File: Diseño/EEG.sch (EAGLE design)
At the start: 19 parts, among them IC1 REF2033AIDDCT

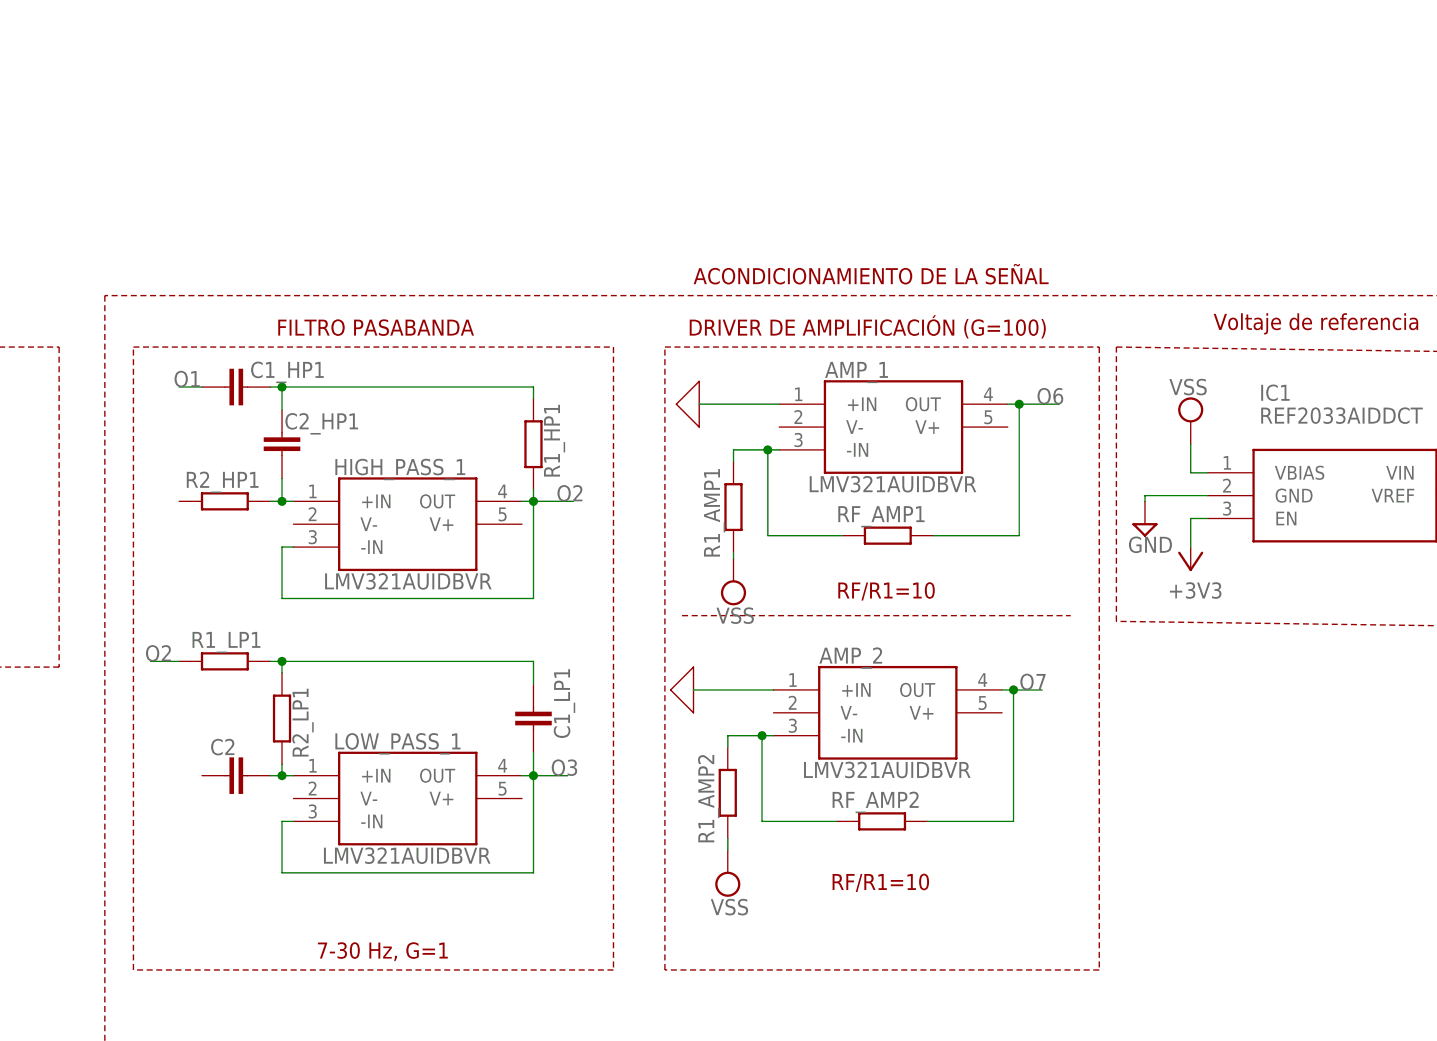
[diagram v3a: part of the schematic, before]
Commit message: correccion de tierras y entradas 3v3 añadidas (cositas varias)    v2
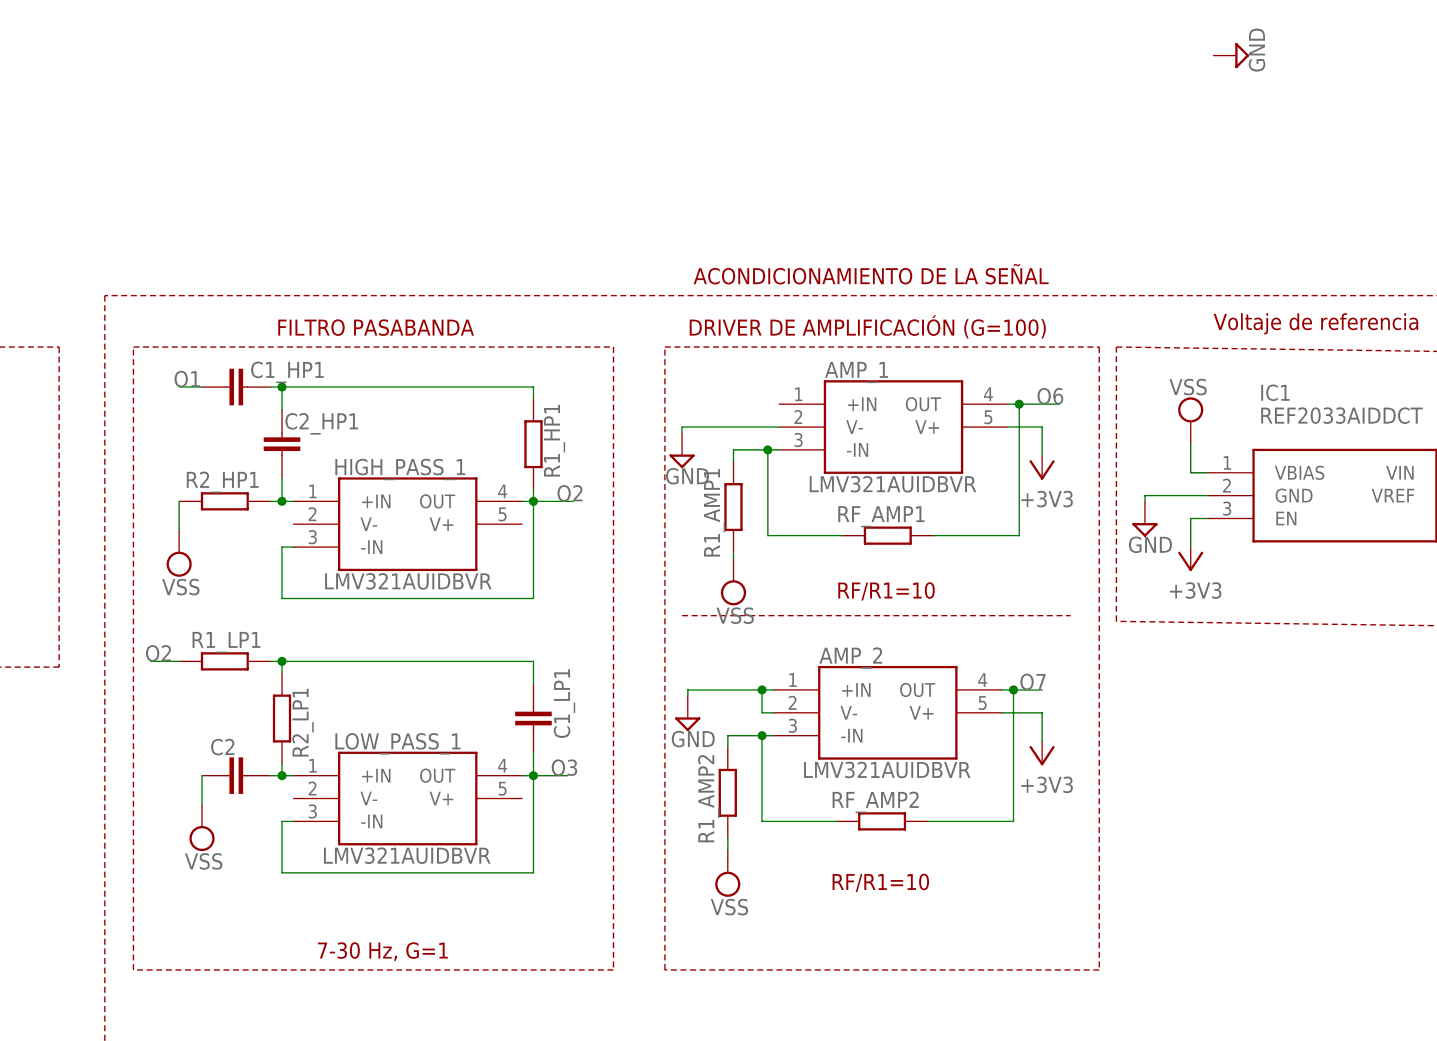
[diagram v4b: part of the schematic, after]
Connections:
- removed net 0: AMP_1.+IN, AMP_2.+IN
- net +3V3: now also AMP_1.V+, AMP_2.V+
- net GND: now also AMP_1.V-, AMP_2.+IN, AMP_2.V-
- net VSS: now also C2.2, R2_HP1.1
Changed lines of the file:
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@@
 <part name="C2" library="rcl" library_urn="urn:adsk.eagle:library:334" deviceset="C-EU" device="C0805" package3d_urn="urn:adsk.eagle:package:23617/2"/>
 <part name="AMP_1" library="LMV321AUIDBVR" deviceset="LMV321AUIDBVR" device=""/>
-<part name="X_1" library="ngspice-simulation" library_urn="urn:adsk.eagle:library:527439" deviceset="GND" device=""/>
 <part name="RF_AMP1" library="rcl" library_urn="urn:adsk.eagle:library:334" deviceset="R-EU_" device="R0805" package3d_urn="urn:adsk.eagle:package:23553/2"/>
 <part name="R1_AMP1" library="rcl" library_urn="urn:adsk.eagle:library:334" deviceset="R-EU_" device="R0805" package3d_urn="urn:adsk.eagle:package:23553/2"/>
 <part name="AMP_2" library="LMV321AUIDBVR" deviceset="LMV321AUIDBVR" device=""/>
-<part name="X_2" library="ngspice-simulation" library_urn="urn:adsk.eagle:library:527439" deviceset="GND" device=""/>
 <part name="RF_AMP2" library="rcl" library_urn="urn:adsk.eagle:library:334" deviceset="R-EU_" device="R0805" package3d_urn="urn:adsk.eagle:package:23553/2"/>
 <part name="R1_AMP2" library="rcl" library_urn="urn:adsk.eagle:library:334" deviceset="R-EU_" device="R0805" package3d_urn="urn:adsk.eagle:package:23553/2"/>
@@
 <part name="SUPPLY3" library="supply2" library_urn="urn:adsk.eagle:library:372" deviceset="VSS" device=""/>
 <part name="SUPPLY4" library="supply2" library_urn="urn:adsk.eagle:library:372" deviceset="VSS" device=""/>
+<part name="SUPPLY5" library="supply2" library_urn="urn:adsk.eagle:library:372" deviceset="GND" device=""/>
+<part name="SUPPLY6" library="supply2" library_urn="urn:adsk.eagle:library:372" deviceset="GND" device=""/>
+<part name="SUPPLY7" library="supply2" library_urn="urn:adsk.eagle:library:372" deviceset="GND" device=""/>
+<part name="+3V3" library="supply1" library_urn="urn:adsk.eagle:library:371" deviceset="+3V3" device=""/>
+<part name="+3V4" library="supply1" library_urn="urn:adsk.eagle:library:371" deviceset="+3V3" device=""/>
+<part name="SUPPLY8" library="supply2" library_urn="urn:adsk.eagle:library:372" deviceset="VSS" device=""/>
+<part name="SUPPLY9" library="supply2" library_urn="urn:adsk.eagle:library:372" deviceset="VSS" device=""/>
 </parts>
 <sheets>
@@
 <attribute name="VALUE" x="151.13" y="153.67" size="1.778" layer="96" align="center-left"/>
 </instance>
-<instance part="X_1" gate="G$1" x="139.065" y="162.56" smashed="yes" rot="R270"/>
 <instance part="RF_AMP1" gate="G$1" x="160.02" y="147.955" smashed="yes">
 <attribute name="NAME" x="154.305" y="149.4536" size="1.778" layer="95"/>
@@
 <attribute name="VALUE" x="150.495" y="121.92" size="1.778" layer="96" align="center-left"/>
 </instance>
-<instance part="X_2" gate="G$1" x="138.43" y="130.81" smashed="yes" rot="R270"/>
 <instance part="RF_AMP2" gate="G$1" x="159.385" y="116.205" smashed="yes">
 <attribute name="NAME" x="153.67" y="117.7036" size="1.778" layer="95"/>
@@
 <instance part="SUPPLY4" gate="G$1" x="142.24" y="110.49" smashed="yes">
 <attribute name="VALUE" x="140.335" y="105.791" size="1.778" layer="96"/>
+</instance>
+<instance part="SUPPLY5" gate="GND" x="198.755" y="201.295" smashed="yes" rot="R90">
+<attribute name="VALUE" x="201.93" y="199.39" size="1.778" layer="96" rot="R90"/>
+</instance>
+<instance part="SUPPLY6" gate="GND" x="137.795" y="127.635" smashed="yes">
+<attribute name="VALUE" x="135.89" y="124.46" size="1.778" layer="96"/>
+</instance>
+<instance part="SUPPLY7" gate="GND" x="137.16" y="156.845" smashed="yes">
+<attribute name="VALUE" x="135.255" y="153.67" size="1.778" layer="96"/>
+</instance>
+<instance part="+3V3" gate="G$1" x="177.165" y="154.305" smashed="yes" rot="R180">
+<attribute name="VALUE" x="174.625" y="151.13" size="1.778" layer="96"/>
+</instance>
+<instance part="+3V4" gate="G$1" x="177.165" y="122.555" smashed="yes" rot="R180">
+<attribute name="VALUE" x="174.625" y="119.38" size="1.778" layer="96"/>
+</instance>
+<instance part="SUPPLY8" gate="G$1" x="81.28" y="146.05" smashed="yes">
+<attribute name="VALUE" x="79.375" y="141.351" size="1.778" layer="96"/>
+</instance>
+<instance part="SUPPLY9" gate="G$1" x="83.82" y="115.57" smashed="yes">
+<attribute name="VALUE" x="81.915" y="110.871" size="1.778" layer="96"/>
 </instance>
 </instances>
@@
 </segment>
 </net>
-<net name="0" class="0">
-<segment>
-<pinref part="AMP_1" gate="G$1" pin="+IN"/>
-<pinref part="X_1" gate="G$1" pin="0"/>
-<wire x1="147.955" y1="162.56" x2="139.065" y2="162.56" width="0.1524" layer="91"/>
-</segment>
-<segment>
-<pinref part="AMP_2" gate="G$1" pin="+IN"/>
-<pinref part="X_2" gate="G$1" pin="0"/>
-<wire x1="147.32" y1="130.81" x2="138.43" y2="130.81" width="0.1524" layer="91"/>
-</segment>
-</net>
 <net name="N$8" class="0">
 <segment>
@@
 <wire x1="142.24" y1="114.3" x2="142.24" y2="113.03" width="0.1524" layer="91"/>
 </segment>
+<segment>
+<pinref part="R2_HP1" gate="G$1" pin="1"/>
+<pinref part="SUPPLY8" gate="G$1" pin="VSS"/>
+<wire x1="81.28" y1="151.765" x2="81.28" y2="148.59" width="0.1524" layer="91"/>
+</segment>
+<segment>
+<pinref part="SUPPLY9" gate="G$1" pin="VSS"/>
+<wire x1="83.82" y1="121.285" x2="83.82" y2="118.11" width="0.1524" layer="91"/>
+<pinref part="C2" gate="G$1" pin="2"/>
+</segment>
 </net>
 <net name="+3V3" class="0">
@@
 <pinref part="IC1" gate="G$1" pin="EN"/>
 </segment>
+<segment>
+<pinref part="+3V3" gate="G$1" pin="+3V3"/>
+<wire x1="177.165" y1="156.845" x2="177.165" y2="160.02" width="0.1524" layer="91"/>
+<pinref part="AMP_1" gate="G$1" pin="V+"/>
+<wire x1="173.355" y1="160.02" x2="177.165" y2="160.02" width="0.1524" layer="91"/>
+</segment>
+<segment>
+<pinref part="+3V4" gate="G$1" pin="+3V3"/>
+<wire x1="177.165" y1="125.095" x2="177.165" y2="128.27" width="0.1524" layer="91"/>
+<pinref part="AMP_2" gate="G$1" pin="V+"/>
+<wire x1="172.72" y1="128.27" x2="177.165" y2="128.27" width="0.1524" layer="91"/>
+</segment>
 </net>
 <net name="GND" class="0">
@@
 <wire x1="188.595" y1="152.4" x2="195.58" y2="152.4" width="0.1524" layer="91"/>
 </segment>
-</net>
+<segment>
+<pinref part="SUPPLY6" gate="GND" pin="GND"/>
+<wire x1="137.795" y1="130.175" x2="137.795" y2="130.81" width="0.1524" layer="91"/>
+<wire x1="137.795" y1="130.81" x2="146.05" y2="130.81" width="0.1524" layer="91"/>
+<pinref part="AMP_2" gate="G$1" pin="+IN"/>
+<pinref part="AMP_2" gate="G$1" pin="V-"/>
+<wire x1="146.05" y1="130.81" x2="147.32" y2="130.81" width="0.1524" layer="91"/>
+<wire x1="147.32" y1="128.27" x2="146.05" y2="128.27" width="0.1524" layer="91"/>
+<wire x1="146.05" y1="128.27" x2="146.05" y2="130.81" width="0.1524" layer="91"/>
+<junction x="146.05" y="130.81"/>
+</segment>
+<segment>
+<pinref part="SUPPLY7" gate="GND" pin="GND"/>
+<wire x1="137.16" y1="159.385" x2="137.16" y2="160.02" width="0.1524" layer="91"/>
+<wire x1="137.16" y1="160.02" x2="147.955" y2="160.02" width="0.1524" layer="91"/>
+<pinref part="AMP_1" gate="G$1" pin="V-"/>
+</segment>
+</net>
